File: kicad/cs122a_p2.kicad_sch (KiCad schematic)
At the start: 15 parts, among them SW1 SW_Tap, SW2 SW_Inc, SW3 SW_Dec, U1 STM32F042K6Tx, U2 Digit 1, U3 Digit 2, U4 Digit 3, U5 SN7447A

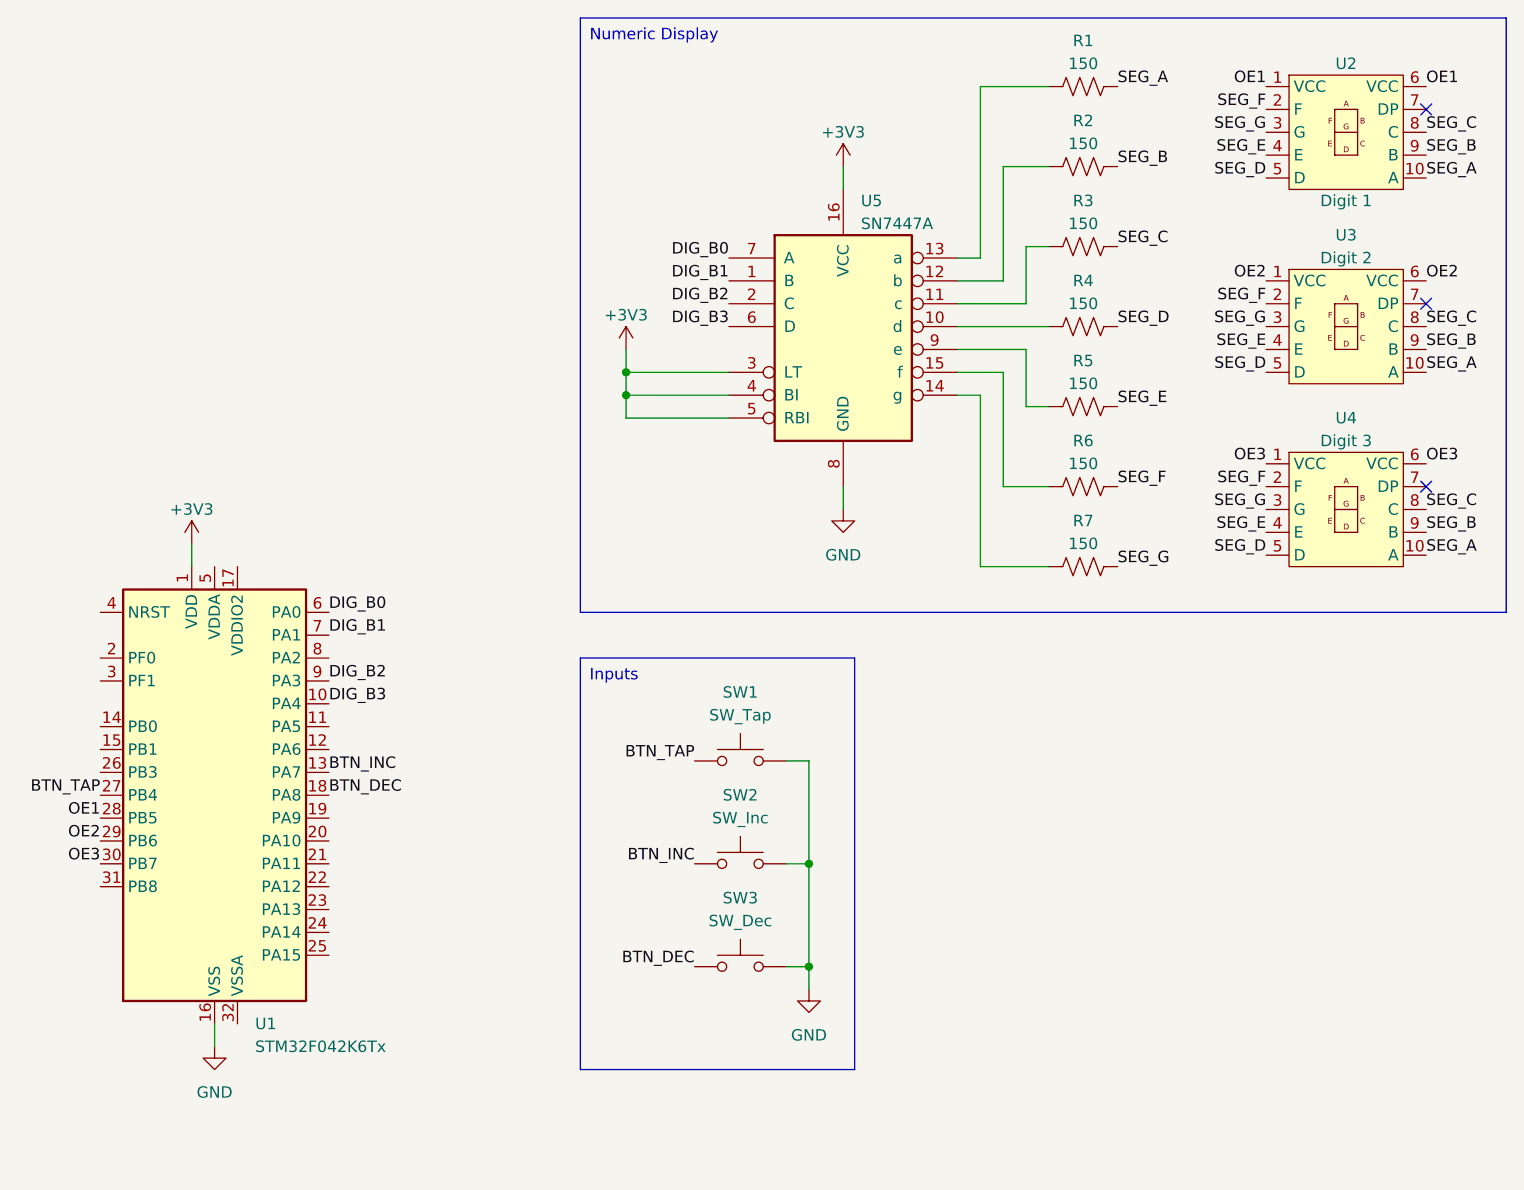
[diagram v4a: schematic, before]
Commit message: Updated schematic to include speaker circuit
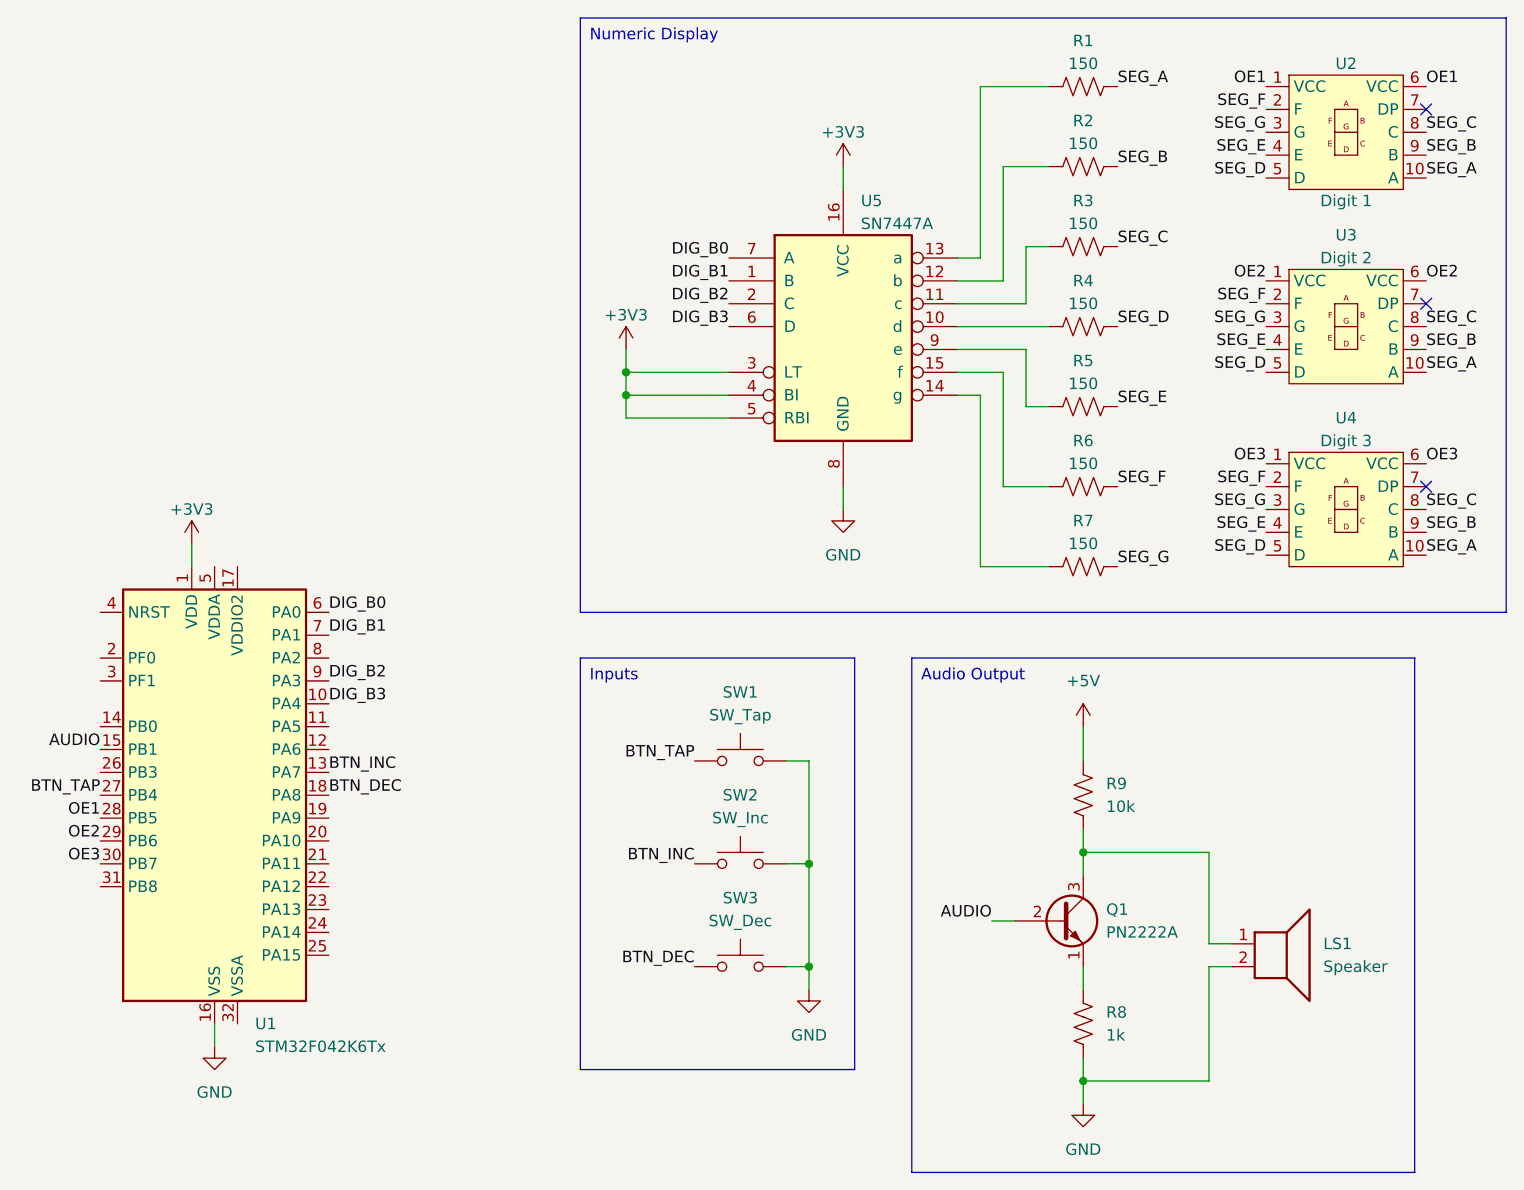
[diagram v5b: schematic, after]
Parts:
- added LS1: Speaker, symbol Device:Speaker
- added Q1: PN2222A, Package_TO_SOT_THT:TO-92_Inline, symbol Transistor_BJT:PN2222A
- added R8: 1k, Resistor_THT:R_Axial_DIN0204_L3.6mm_D1.6mm_P7.62mm_Horizontal, symbol Device:R_US
- added R9: 10k, Resistor_THT:R_Axial_DIN0204_L3.6mm_D1.6mm_P7.62mm_Horizontal, symbol Device:R_US
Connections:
- net GND: now also LS1.2, R8.2
- net AUDIO: now reaches U1.15 (PB1)
- net AUDIO: now also Q1.2 (B)
- new net: Q1.1 (E), R8.1
- new net: LS1.1, Q1.3 (C), R9.2
- new net +5V: R9.1
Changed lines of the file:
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@@
   (junction (at 201.93 111.76) (diameter 0) (color 0 0 0 0)
+  )
+  (junction (at 232.41 135.89) (diameter 0) (color 0 0 0 0)
+  )
+  (junction (at 232.41 110.49) (diameter 0) (color 0 0 0 0)
   )
   (junction (at 181.61 59.69) (diameter 0) (color 0 0 0 0)
@@
     (stroke (width 0) (type default))
   )
+  (wire (pts (xy 246.38 123.19) (xy 246.38 135.89))
+    (stroke (width 0) (type default))
+  )
   (wire (pts (xy 199.39 111.76) (xy 201.93 111.76))
     (stroke (width 0) (type default))
   )
+  (wire (pts (xy 232.41 135.89) (xy 232.41 133.35))
+    (stroke (width 0) (type default))
+  )
   (wire (pts (xy 201.93 125.73) (xy 201.93 123.19))
     (stroke (width 0) (type default))
@@
     (stroke (width 0) (type default))
   )
+  (wire (pts (xy 246.38 123.19) (xy 248.92 123.19))
+    (stroke (width 0) (type default))
+  )
   (wire (pts (xy 220.98 78.74) (xy 228.6 78.74))
     (stroke (width 0) (type default))
   )
+  (wire (pts (xy 232.41 125.73) (xy 232.41 123.19))
+    (stroke (width 0) (type default))
+  )
   (wire (pts (xy 201.93 111.76) (xy 201.93 123.19))
     (stroke (width 0) (type default))
   )
+  (wire (pts (xy 246.38 120.65) (xy 248.92 120.65))
+    (stroke (width 0) (type default))
+  )
   (wire (pts (xy 228.6 34.29) (xy 223.52 34.29))
     (stroke (width 0) (type default))
   )
+  (wire (pts (xy 246.38 135.89) (xy 232.41 135.89))
+    (stroke (width 0) (type default))
+  )
   (wire (pts (xy 218.44 49.53) (xy 226.06 49.53))
     (stroke (width 0) (type default))
   )
+  (wire (pts (xy 232.41 138.43) (xy 232.41 135.89))
+    (stroke (width 0) (type default))
+  )
   (wire (pts (xy 226.06 60.96) (xy 228.6 60.96))
     (stroke (width 0) (type default))
@@
     (stroke (width 0) (type default))
   )
+  (wire (pts (xy 222.25 118.11) (xy 224.79 118.11))
+    (stroke (width 0) (type default))
+  )
+  (wire (pts (xy 232.41 96.52) (xy 232.41 100.33))
+    (stroke (width 0) (type default))
+  )
+  (wire (pts (xy 246.38 120.65) (xy 246.38 110.49))
+    (stroke (width 0) (type default))
+  )
   (wire (pts (xy 199.39 100.33) (xy 201.93 100.33))
     (stroke (width 0) (type default))
@@
     (stroke (width 0) (type default))
   )
+  (wire (pts (xy 246.38 110.49) (xy 232.41 110.49))
+    (stroke (width 0) (type default))
+  )
   (wire (pts (xy 133.35 76.2) (xy 133.35 78.74))
     (stroke (width 0) (type default))
@@
   )
   (wire (pts (xy 218.44 54.61) (xy 226.06 54.61))
+    (stroke (width 0) (type default))
+  )
+  (wire (pts (xy 232.41 110.49) (xy 232.41 113.03))
+    (stroke (width 0) (type default))
+  )
+  (wire (pts (xy 232.41 107.95) (xy 232.41 110.49))
     (stroke (width 0) (type default))
   )
@@
     (effects (font (size 1.27 1.27)) (justify left top))
   )
+  (text_box "Audio Output"
+    (at 213.36 88.9 0) (size 55.88 57.15)
+    (stroke (width 0) (type default))
+    (fill (type none))
+    (effects (font (size 1.27 1.27)) (justify left top))
+  )
   (label "BTN_DEC" (at 148.59 104.14 0) (fields_autoplaced)
     (effects (font (size 1.27 1.27)) (justify left bottom))
@@
     (effects (font (size 1.27 1.27)) (justify right bottom))
   )
+  (label "AUDIO" (at 123.19 99.06 180) (fields_autoplaced)
+    (effects (font (size 1.27 1.27)) (justify right bottom))
+  )
   (label "BTN_INC" (at 148.59 101.6 0) (fields_autoplaced)
     (effects (font (size 1.27 1.27)) (justify left bottom))
@@
   )
   (label "SEG_D" (at 252.73 35.56 180) (fields_autoplaced)
+    (effects (font (size 1.27 1.27)) (justify right bottom))
+  )
+  (label "AUDIO" (at 222.25 118.11 180) (fields_autoplaced)
     (effects (font (size 1.27 1.27)) (justify right bottom))
   )
@@
     )
   )
+  (symbol (lib_id "Device:R_US") (at 232.41 129.54 0) (unit 1)
+    (in_bom yes) (on_board yes) (dnp no) (fields_autoplaced)
+    (property "Reference" "R8" (at 234.95 128.27 0)
+      (effects (font (size 1.27 1.27)) (justify left))
+    )
+    (property "Value" "1k" (at 234.95 130.81 0)
+      (effects (font (size 1.27 1.27)) (justify left))
+    )
+    (property "Footprint" "Resistor_THT:R_Axial_DIN0204_L3.6mm_D1.6mm_P7.62mm_Horizontal" (at 233.426 129.794 90)
+      (effects (font (size 1.27 1.27)) hide)
+    )
+    (property "Datasheet" "~" (at 232.41 129.54 0)
+      (effects (font (size 1.27 1.27)) hide)
+    )
+    (pin "1")
+    (pin "2")
+    (instances
+      (project "cs122a_p2"
+        (path "/f5250a06-5d3f-42a4-81bc-c043e883a187"
+          (reference "R8") (unit 1)
+        )
+      )
+    )
+  )
   (symbol (lib_id "power:GND") (at 205.74 72.39 0) (unit 1)
     (in_bom yes) (on_board yes) (dnp no) (fields_autoplaced)
@@
     )
   )
+  (symbol (lib_id "Device:Speaker") (at 254 120.65 0) (unit 1)
+    (in_bom yes) (on_board yes) (dnp no) (fields_autoplaced)
+    (property "Reference" "LS1" (at 259.08 120.65 0)
+      (effects (font (size 1.27 1.27)) (justify left))
+    )
+    (property "Value" "Speaker" (at 259.08 123.19 0)
+      (effects (font (size 1.27 1.27)) (justify left))
+    )
+    (property "Footprint" "" (at 254 125.73 0)
+      (effects (font (size 1.27 1.27)) hide)
+    )
+    (property "Datasheet" "~" (at 253.746 121.92 0)
+      (effects (font (size 1.27 1.27)) hide)
+    )
+    (pin "1")
+    (pin "2")
+    (instances
+      (project "cs122a_p2"
+        (path "/f5250a06-5d3f-42a4-81bc-c043e883a187"
+          (reference "LS1") (unit 1)
+        )
+      )
+    )
+  )
+  (symbol (lib_id "power:GND") (at 232.41 138.43 0) (unit 1)
+    (in_bom yes) (on_board yes) (dnp no) (fields_autoplaced)
+    (property "Reference" "#PWR08" (at 232.41 144.78 0)
+      (effects (font (size 1.27 1.27)) hide)
+    )
+    (property "Value" "GND" (at 232.41 143.51 0)
+      (effects (font (size 1.27 1.27)))
+    )
+    (property "Footprint" "" (at 232.41 138.43 0)
+      (effects (font (size 1.27 1.27)) hide)
+    )
+    (property "Datasheet" "" (at 232.41 138.43 0)
+      (effects (font (size 1.27 1.27)) hide)
+    )
+    (pin "1")
+    (instances
+      (project "cs122a_p2"
+        (path "/f5250a06-5d3f-42a4-81bc-c043e883a187"
+          (reference "#PWR08") (unit 1)
+        )
+      )
+    )
+  )
+  (symbol (lib_id "Transistor_BJT:PN2222A") (at 229.87 118.11 0) (unit 1)
+    (in_bom yes) (on_board yes) (dnp no) (fields_autoplaced)
+    (property "Reference" "Q1" (at 234.95 116.84 0)
+      (effects (font (size 1.27 1.27)) (justify left))
+    )
+    (property "Value" "PN2222A" (at 234.95 119.38 0)
+      (effects (font (size 1.27 1.27)) (justify left))
+    )
+    (property "Footprint" "Package_TO_SOT_THT:TO-92_Inline" (at 234.95 120.015 0)
+      (effects (font (size 1.27 1.27) italic) (justify left) hide)
+    )
+    (property "Datasheet" "https://www.onsemi.com/pub/Collateral/PN2222-D.PDF" (at 229.87 118.11 0)
+      (effects (font (size 1.27 1.27)) (justify left) hide)
+    )
+    (pin "1")
+    (pin "2")
+    (pin "3")
+    (instances
+      (project "cs122a_p2"
+        (path "/f5250a06-5d3f-42a4-81bc-c043e883a187"
+          (reference "Q1") (unit 1)
+        )
+      )
+    )
+  )
   (symbol (lib_id "74xx:74LS47") (at 205.74 52.07 0) (unit 1)
     (in_bom yes) (on_board yes) (dnp no) (fields_autoplaced)
@@
         (path "/f5250a06-5d3f-42a4-81bc-c043e883a187"
           (reference "U5") (unit 1)
+        )
+      )
+    )
+  )
+  (symbol (lib_id "power:+5V") (at 232.41 96.52 0) (unit 1)
+    (in_bom yes) (on_board yes) (dnp no) (fields_autoplaced)
+    (property "Reference" "#PWR07" (at 232.41 100.33 0)
+      (effects (font (size 1.27 1.27)) hide)
+    )
+    (property "Value" "+5V" (at 232.41 91.44 0)
+      (effects (font (size 1.27 1.27)))
+    )
+    (property "Footprint" "" (at 232.41 96.52 0)
+      (effects (font (size 1.27 1.27)) hide)
+    )
+    (property "Datasheet" "" (at 232.41 96.52 0)
+      (effects (font (size 1.27 1.27)) hide)
+    )
+    (pin "1")
+    (instances
+      (project "cs122a_p2"
+        (path "/f5250a06-5d3f-42a4-81bc-c043e883a187"
+          (reference "#PWR07") (unit 1)
         )
       )
@@
         )
       )
+    )
+  )
+  (symbol (lib_id "Device:R_US") (at 232.41 104.14 0) (unit 1)
+    (in_bom yes) (on_board yes) (dnp no) (fields_autoplaced)
+    (property "Reference" "R9" (at 234.95 102.87 0)
+      (effects (font (size 1.27 1.27)) (justify left))
+    )
+    (property "Value" "10k" (at 234.95 105.41 0)
+      (effects (font (size 1.27 1.27)) (justify left))
+    )
+    (property "Footprint" "Resistor_THT:R_Axial_DIN0204_L3.6mm_D1.6mm_P7.62mm_Horizontal" (at 233.426 104.394 90)
+      (effects (font (size 1.27 1.27)) hide)
+    )
+    (property "Datasheet" "~" (at 232.41 104.14 0)
+      (effects (font (size 1.27 1.27)) hide)
+    )
+    (pin "1")
+    (pin "2")
+    (instances
+      (project "cs122a_p2"
+        (path "/f5250a06-5d3f-42a4-81bc-c043e883a187"
+          (reference "R9") (unit 1)
+        )
+      )
